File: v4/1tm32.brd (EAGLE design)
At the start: 50.8 x 50.8 mm, 50 parts, among them IC1 STM32L412RBT6P, J2 10118192-0001LF, SW1 LL3301FF065QJ, U2 LD39050PU33R, Y1 8MHz, Y2 32.7KHz

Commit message: added labels for header pins
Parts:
- moved R7 0.76 mm to (34.0, 40.5)
- moved R11 0.51 mm to (9.91, 27.4)
- moved R5 0.51 mm to (9.91, 24.9)
- moved JP2 0.51 mm to (5.08, 26.2)
- moved JP5 0.51 mm to (5.08, 32.8)
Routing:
- net TIM2_CH4: track 35.1 -> 32.3 mm
- net TIM2_CH3: track 31.5 -> 28.7 mm
- net TIM2_CH1: track 28.5 -> 25.9 mm
- net TIM16_CH1: track 27.7 -> 25.1 mm
- net TIM15_CH1: track 26.7 -> 24.3 mm
- net TIM2_CH2: track 26.3 -> 23.9 mm
- net TIM15_CH2: track 19.2 -> 20.7 mm
- net 5V: track 112.6 -> 111.8 mm
- net TIM1_CH1: track 20.7 -> 21.5 mm
- net 3V3: track 82.2 -> 81.5 mm
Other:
- board text added: "3V3"
- board text added: "5V"
- board text added: "5V_IN"
- board text added: "ADC_8"
- board text added: "ADC_9"
- board text added: "BOOT"
- board text added: "GND"
- board text added: "I2C1"
- board text added: "I2C2"
- board text added: "I2C3"
- board text added: "LED_R"
- board text added: "NRST"
- board text added: "RX"
- board text added: "SWCLK"
- board text added: "SWDIO"
- board text added: "SWO"
- board text added: "T15_1"
- board text added: "T15_2"
- board text added: "T16_1"
- board text added: "T1_1"
- board text added: "T1_2"
- board text added: "T1_3"
- board text added: "T1_4"
- board text added: "T2_1"
- board text added: "T2_2"
- board text added: "T2_3"
- board text added: "T2_4"
- board text added: "TX"
- board text added: "UART1"
- board text added: "UART3"

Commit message: modified i2c headers
removed resistors
changed 3v3 pins to gpio pins
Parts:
- removed R12, R13, R2, R3, R8, R9: 1K, RC0805FR-131KL:RESC2012X60N
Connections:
- new net PC4: IC1.24, JP1.5
- new net PC5: IC1.25, JP1.7
- net 3V3: no longer JP1.5, JP1.7, R12.1, R13.1, R2.2, R3.2, R8.2, R9.2
- net I2C1_SCL: no longer R9.1
- net I2C1_SDA: no longer R8.1
- net I2C2_SCL: no longer R2.1
- net I2C2_SDA: no longer R3.1
- net I2C3_SCL: no longer R13.2
- net I2C3_SDA: no longer R12.2
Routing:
- net 3V3: track 81.5 -> 61.4 mm, vias 13 -> 10
- net PC5: track 0.00 -> 19.3 mm, vias 0 -> 2
- net PC4: track 0.00 -> 19.1 mm, vias 0 -> 2
- net I2C2_SCL: track 27.5 -> 23.2 mm
- net I2C3_SCL: track 32.7 -> 29.7 mm
- net I2C2_SDA: track 28.1 -> 26.0 mm
- net I2C1_SDA: track 31.1 -> 29.6 mm
- net TIM2_CH4: track 32.3 -> 33.8 mm
- net 5V: track 111.8 -> 110.7 mm
- net I2C3_SDA: track 31.6 -> 30.6 mm
- net I2C1_SCL: track 31.0 -> 30.1 mm
- net TIM2_CH3: track 28.7 -> 29.5 mm

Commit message: moved some wires around
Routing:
- net I2C3_SDA: track 30.6 -> 29.1 mm
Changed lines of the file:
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@@
 <wire x1="21.857" y1="13.398" x2="15.93" y2="13.398" width="0.2032" layer="1"/>
 <wire x1="15.93" y1="13.398" x2="15.913" y2="13.381" width="0.2032" layer="1"/>
-<wire x1="38.862" y1="32.258" x2="46.736" y2="26.162" width="0" layer="19" extent="1-1"/>
-<wire x1="22.443" y1="31.482" x2="31.931" y2="29.494" width="0" layer="19" extent="1-1"/>
-<wire x1="18.923" y1="38.481" x2="20.193" y2="37.3858" width="0" layer="19" extent="1-1"/>
-<wire x1="20.193" y1="47.117" x2="19.731" y2="39.665" width="0" layer="19" extent="1-1"/>
-<wire x1="29.943" y1="20.006" x2="31.931" y2="29.494" width="0" layer="19" extent="1-1"/>
-<wire x1="23.443" y1="20.006" x2="29.943" y2="20.006" width="0" layer="19" extent="1-1"/>
-<wire x1="34.45" y1="9.7" x2="32.766" y2="16.383" width="0" layer="19" extent="1-1"/>
 </signal>
 <signal name="USART1_RX">
@@
 <wire x1="20.359" y1="25.398" x2="19.6122875" y2="25.398" width="0.2032" layer="1"/>
 <wire x1="19.6122875" y1="25.398" x2="19.3602875" y2="25.146" width="0.2032" layer="1"/>
-<wire x1="15.1079" y1="25.146" x2="11.6951" y2="21.7332" width="0.2032" layer="1"/>
-<wire x1="10.8112" y1="21.7332" x2="10.414" y2="21.336" width="0.2032" layer="1"/>
-<wire x1="11.6951" y1="21.7332" x2="10.8112" y2="21.7332" width="0.2032" layer="1"/>
-<wire x1="10.414" y1="21.336" x2="10.414" y2="13.2689" width="0.2032" layer="1"/>
+<wire x1="15.1079" y1="25.146" x2="10.541" y2="20.5791" width="0.2032" layer="1"/>
+<wire x1="10.541" y1="20.5791" x2="10.541" y2="13.0302125" width="0.2032" layer="1"/>
 <wire x1="19.3602875" y1="25.146" x2="15.1079" y2="25.146" width="0.2032" layer="1"/>
-<wire x1="13.8709" y1="9.812" x2="15.2832125" y2="9.812" width="0.2032" layer="1"/>
-<wire x1="10.414" y1="13.2689" x2="13.8709" y2="9.812" width="0.2032" layer="1"/>
-<wire x1="17.018" y1="8.0772125" x2="17.018" y2="6.096" width="0.2032" layer="1"/>
-<wire x1="15.2832125" y1="9.812" x2="17.018" y2="8.0772125" width="0.2032" layer="1"/>
+<wire x1="10.541" y1="13.0302125" x2="17.018" y2="6.5532125" width="0.2032" layer="1"/>
+<wire x1="17.018" y1="6.5532125" x2="17.018" y2="6.096" width="0.2032" layer="1"/>
 </signal>
 <signal name="TIM15_CH1">

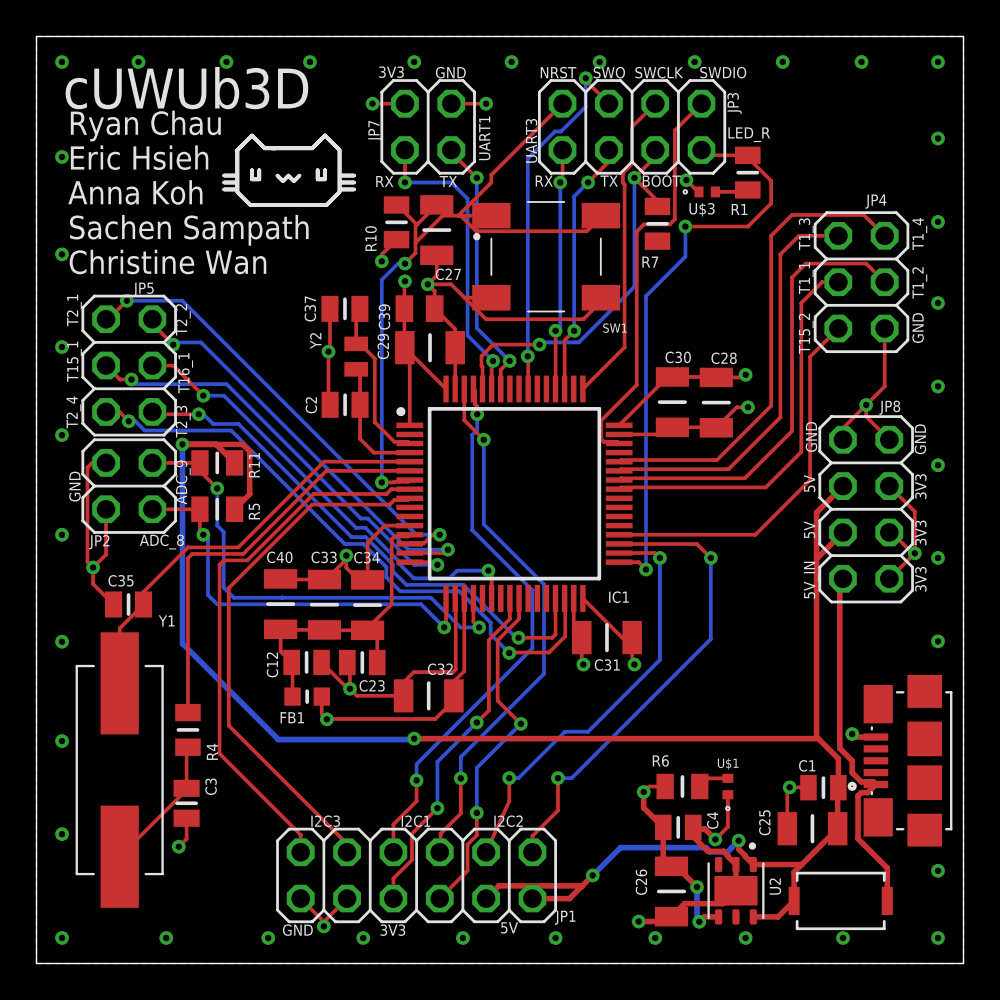
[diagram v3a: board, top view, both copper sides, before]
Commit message: moved wire around to space for pwm wave
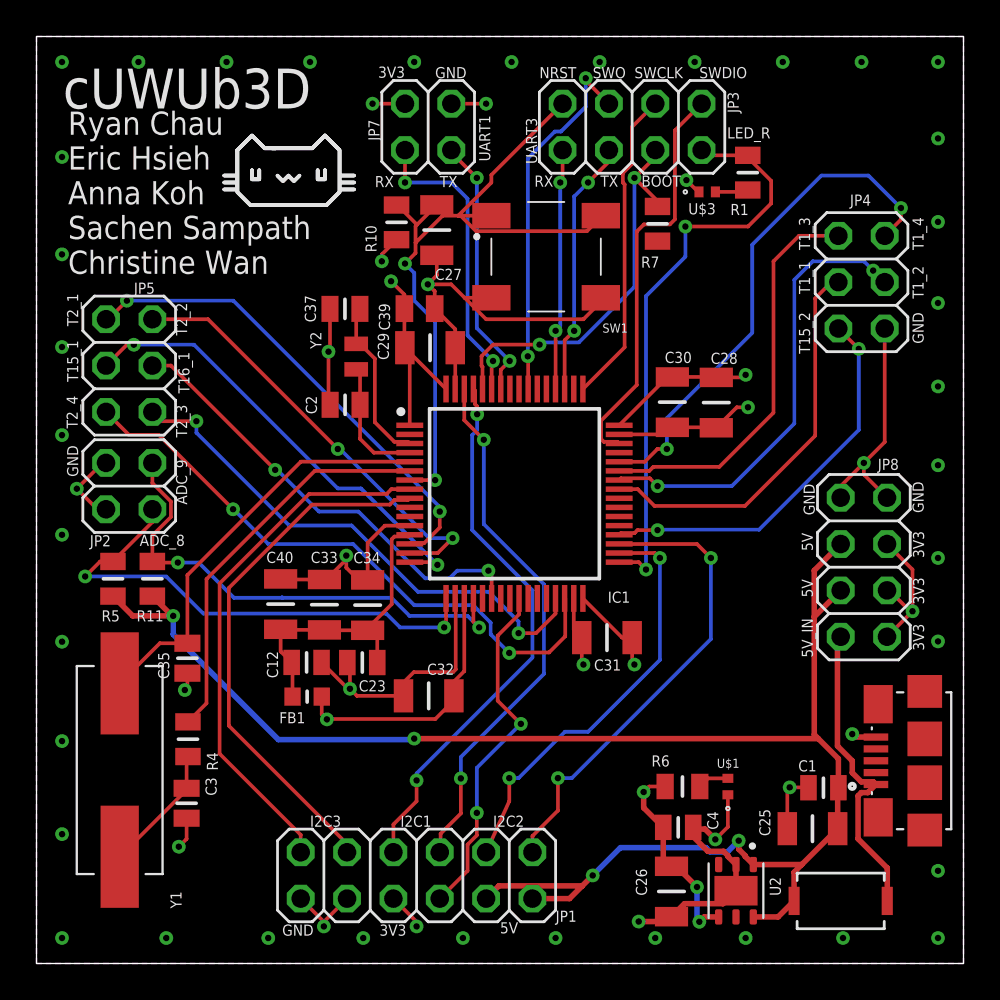
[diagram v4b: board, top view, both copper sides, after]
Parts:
- moved R11 7.28 mm to (6.35, 21.1), turned to 90 degrees
- moved R5 6.87 mm to (4.19, 21.1), turned to 90 degrees
- moved C35 4.36 mm to (8.27, 16.7), turned to 270 degrees
- moved JP8 3.18 mm to (45.3, 21.7)
- moved R4 0.51 mm to (8.30, 12.3)
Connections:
- net 3V3: now also JP1.5
- net PC4: no longer JP1.5
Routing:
- net PC4: track 19.1 -> 0.00 mm, vias 2 -> 0
- net 5V: track 110.7 -> 93.1 mm
- net ADC2_IN8: track 22.8 -> 28.1 mm
- net GND: track 113.6 -> 109.4 mm, vias 53 -> 54
- net 5V_IN: track 20.2 -> 17.1 mm
- net 3V3: track 61.4 -> 63.7 mm, vias 10 -> 11
- net TIM1_CH4: track 26.1 -> 28.4 mm, vias 0 -> 2
- net TIM15_CH1: track 24.3 -> 25.2 mm
- net TIM15_CH2: track 20.7 -> 21.5 mm, vias 0 -> 2
- net ADC1_IN9: track 26.6 -> 27.4 mm
- net PH1-OSC-OUT: track 22.6 -> 21.8 mm
- net TIM2_CH1: track 25.9 -> 26.5 mm
- net I2C3_SCL: track 29.7 -> 29.1 mm
- net N$3: track 7.55 -> 7.04 mm
- net TIM1_CH2: track 24.8 -> 25.0 mm, vias 0 -> 2
